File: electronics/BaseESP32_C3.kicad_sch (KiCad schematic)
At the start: 15 parts, among them J10 Conn_01x07, J11 Boot jumper, U1 ESP32-C3-MINI-1-N4

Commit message: Bollard orientation USB/JST, updated designators
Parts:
- D6: Farnell 2322102 -> (none); Farnell Price/Stock https://uk.farnell.com/multicomp-pro/mp008279/led-green-70m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 -> (none); LCSC C601686 -> C965815; LCSC Stock (none) -> https://jlcpcb.com/partdetail/Xinglight-XL2012UGC/C965815
- R12: Farnell 2502470 -> (none); Farnell Price/Stock https://uk.farnell.com/walsin/wr06x5600ftl/res-560r-1-75v-0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 -> (none); LCSC C20573 -> C163460
- R15, R16: Farnell 3495168 -> (none); Farnell Price/Stock https://uk.farnell.com/yageo/ac0201fr-0722rl/res-22r-1-0-05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 -> (none); LCSC C5139642 -> C25092; LCSC Stock (none) -> https://jlcpcb.com/partdetail/25835-0402WGF220JTCE/C25092
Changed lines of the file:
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@@
 			)
 		)
-		(property "Farnell" "3495168 "
+		(property "Farnell" ""
 			(at 173.99 152.4 0)
 			(effects
@@
 			)
 		)
-		(property "Farnell Price/Stock" "https://uk.farnell.com/yageo/ac0201fr-0722rl/res-22r-1-0-05w-0201-thick-film/dp/3495168"
+		(property "Farnell Price/Stock" ""
 			(at 173.99 152.4 0)
 			(effects
@@
 			)
 		)
-		(property "LCSC" "C5139642"
+		(property "LCSC" "C25092"
 			(at 173.99 152.4 0)
 			(effects
@@
 			)
 		)
-		(property "LCSC Stock" ""
+		(property "LCSC Stock" "https://jlcpcb.com/partdetail/25835-0402WGF220JTCE/C25092"
 			(at 173.99 152.4 0)
 			(effects
@@
 			)
 		)
-		(property "Farnell" "2502470"
+		(property "Farnell" ""
 			(at 195.58 121.92 90)
 			(effects
@@
 			)
 		)
-		(property "Farnell Price/Stock" "https://uk.farnell.com/walsin/wr06x5600ftl/res-560r-1-75v-0603-thick-film/dp/2502470"
+		(property "Farnell Price/Stock" ""
 			(at 195.58 121.92 90)
 			(effects
@@
 			)
 		)
-		(property "LCSC" "C20573"
+		(property "LCSC" "C163460"
 			(at 195.58 121.92 90)
 			(effects
@@
 			)
 		)
-		(property "Farnell" "3495168 "
+		(property "Farnell" ""
 			(at 146.05 152.4 0)
 			(effects
@@
 			)
 		)
-		(property "Farnell Price/Stock" "https://uk.farnell.com/yageo/ac0201fr-0722rl/res-22r-1-0-05w-0201-thick-film/dp/3495168"
+		(property "Farnell Price/Stock" ""
 			(at 146.05 152.4 0)
 			(effects
@@
 			)
 		)
-		(property "LCSC" "C5139642"
+		(property "LCSC" "     C25092"
 			(at 146.05 152.4 0)
 			(effects
@@
 			)
 		)
-		(property "LCSC Stock" ""
+		(property "LCSC Stock" "https://jlcpcb.com/partdetail/25835-0402WGF220JTCE/C25092"
 			(at 146.05 152.4 0)
 			(effects
@@
 			)
 		)
-		(property "Description" ""
+		(property "Description" "0805 Standard led Green"
 			(at 195.58 111.76 0)
 			(effects
@@
 			)
 		)
-		(property "Farnell" "2322102"
+		(property "Farnell" ""
 			(at 195.58 111.76 0)
 			(effects
@@
 			)
 		)
-		(property "Farnell Price/Stock" "https://uk.farnell.com/multicomp-pro/mp008279/led-green-70mcd-576nm-0805/dp/3796308"
+		(property "Farnell Price/Stock" ""
 			(at 195.58 111.76 0)
 			(effects
@@
 			)
 		)
-		(property "LCSC" "C601686"
+		(property "LCSC" "C965815"
 			(at 195.58 111.76 0)
 			(effects
@@
 			)
 		)
-		(property "LCSC Stock" ""
+		(property "LCSC Stock" "https://jlcpcb.com/partdetail/Xinglight-XL2012UGC/C965815"
 			(at 195.58 111.76 0)
 			(effects

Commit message: Fixed designators to match up same parts
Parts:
- R15: LCSC C25092 -> C25092
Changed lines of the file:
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@@
 			)
 		)
-		(property "LCSC" "     C25092"
+		(property "LCSC" "C25092"
 			(at 146.05 152.4 0)
 			(effects

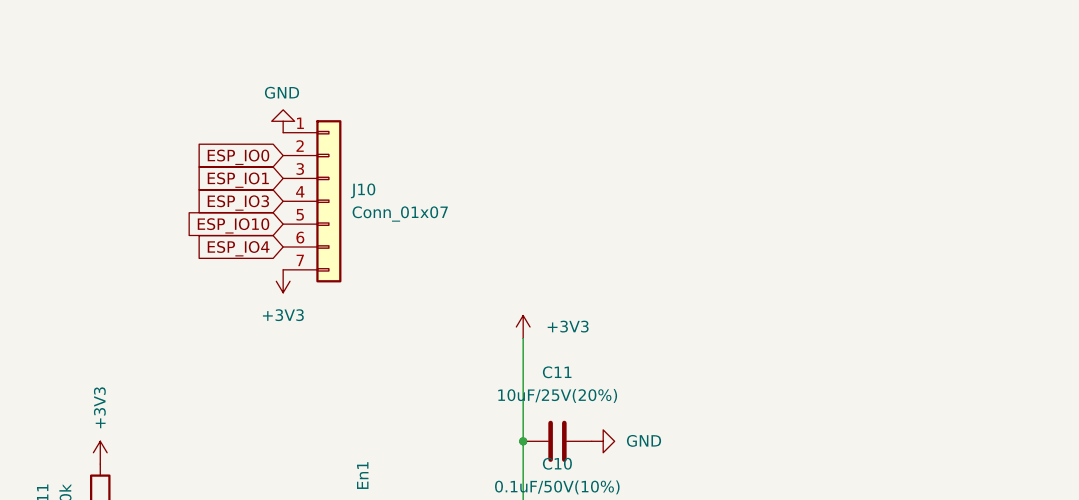
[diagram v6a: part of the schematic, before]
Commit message: Updated silkscreen and readme for microphone version of the board
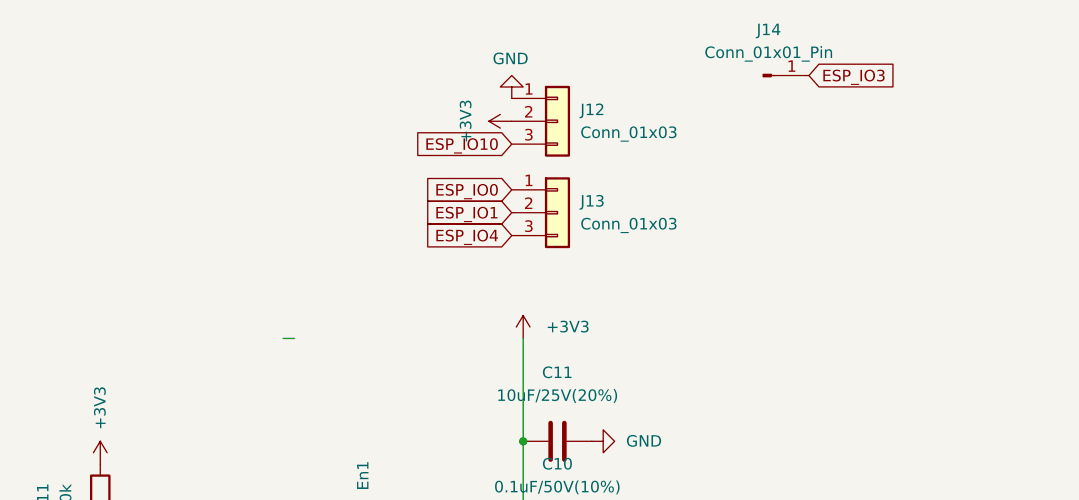
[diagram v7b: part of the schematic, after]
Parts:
- removed J10: Conn_01x07, Connector_PinHeader_2.54mm:PinHeader_1x07_P2.54mm_Vertical, symbol Connector_Generic:Conn_01x07
- added J12, J13: Conn_01x03, Connector_PinHeader_2.54mm:PinHeader_1x03_P2.54mm_Vertical, symbol Connector_Generic:Conn_01x03
- added J14: Conn_01x01_Pin, Connector_PinHeader_2.54mm:PinHeader_1x01_P2.54mm_Vertical, symbol Connector:Conn_01x01_Pin
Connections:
- net +3V3: now also J12.2 (Pin_2)
- net ESP_IO0: now also J13.1 (Pin_1)
- net ESP_IO1: now also J13.2 (Pin_2)
- net ESP_IO10: now also J12.3 (Pin_3)
- net ESP_IO3: now also J14.1 (Pin_1)
- net ESP_IO4: now also J13.3 (Pin_3)
- net GND: now also J12.1 (Pin_1)
